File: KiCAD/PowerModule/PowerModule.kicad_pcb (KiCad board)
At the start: 2 copper layers, 90 x 70 mm, 59 parts, among them J2 BATTERY, J3 BUS, J4 MONITOR, Q1 TK8S06K3L, Q2 TK8S06K3L, Q3 AO3401A, Q5 AO3401A, U2 INA219BxDCN, U3 INA219BxDCN, U4 INA219BxDCN, U5 NJM7812SDL1, U6 NJM7812SDL1, U7 NJM7812SDL1, U8 INA219BxDCN

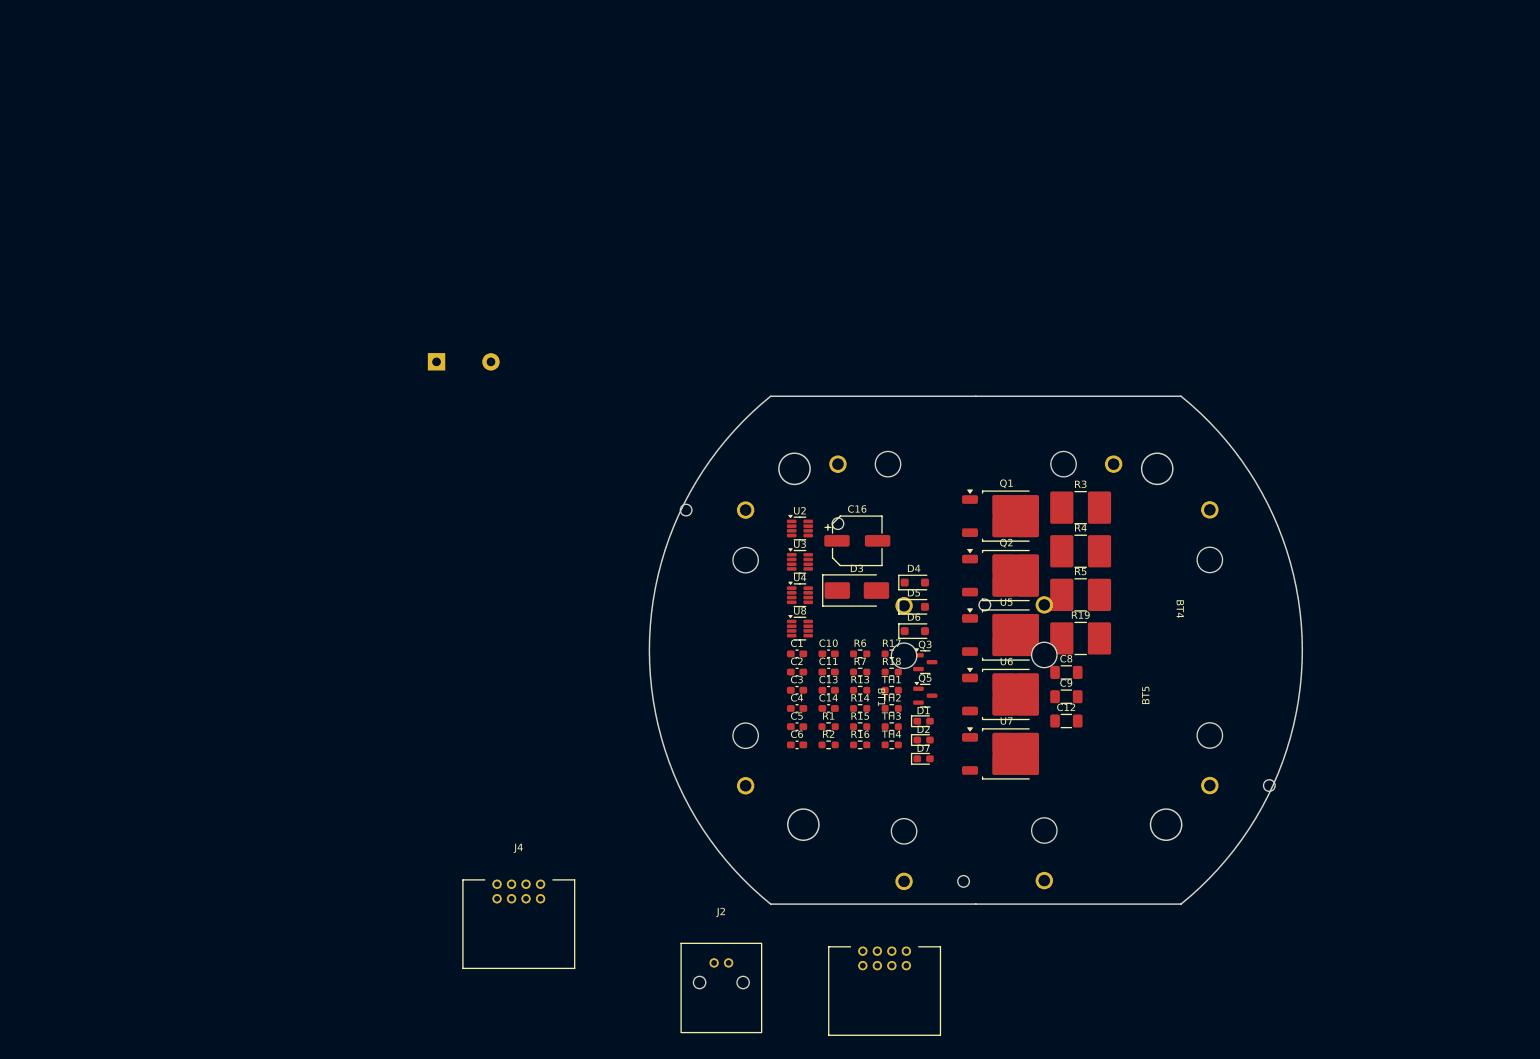
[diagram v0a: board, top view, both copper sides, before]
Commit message: BatteryModule追加＆電池設置
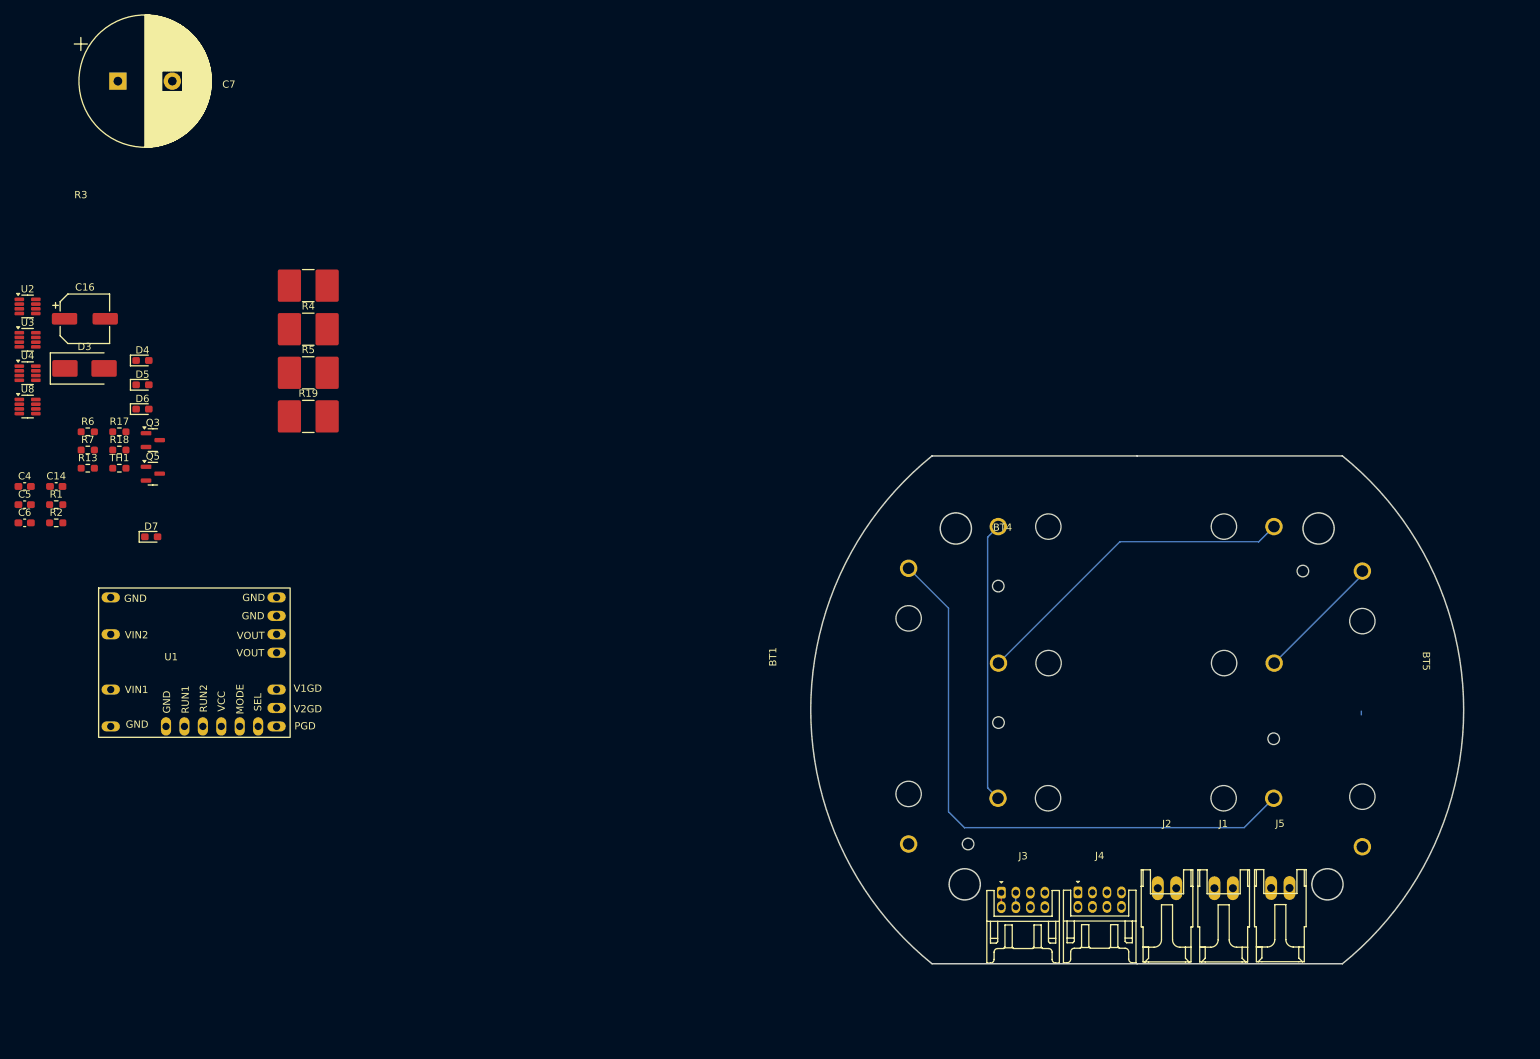
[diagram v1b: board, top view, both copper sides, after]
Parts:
- removed C1, C10, C11, C13: 0.1uF, Capacitor_SMD:C_0603_1608Metric_Pad1.08x0.95mm_HandSolder
- removed C12, C8, C9: 10uF, Capacitor_SMD:C_1206_3216Metric_Pad1.33x1.80mm_HandSolder
- removed C2, C3: 0.056uF, Capacitor_SMD:C_0603_1608Metric_Pad1.08x0.95mm_HandSolder
- removed D1, D2: Orange, LED_SMD:LED_0603_1608Metric_Pad1.05x0.95mm_HandSolder
- removed Q1, Q2: TK8S06K3L, Package_TO_SOT_SMD:TO-252-2
- removed R14, R15, R16, TH2, TH3, TH4: 10kR, Resistor_SMD:R_0603_1608Metric_Pad0.98x0.95mm_HandSolder
- removed U5, U6, U7: NJM7812SDL1, Package_TO_SOT_SMD:TO-252-2
- added J1: GPU, TSRP_Connector_Hirose:DF1B-2S-2.5R, F.Cu at (183.3, 134.4)
- added J5: MASTER, TSRP_Connector_Hirose:DF1B-2S-2.5R, F.Cu at (191.1, 134.4)
- added U1: ~, TSRP_IC:StrawberryLinux_LTC3118, F.Cu at (38.3, 102.3)
- C7: moved to F.Cu
- D4, D5, D6: value GS1010FL -> Orange; footprint Diode_SMD:D_SOD-123F -> LED_SMD:LED_0603_1608Metric_Pad1.05x0.95mm_HandSolder
- J2: footprint TSRP_Connector_Hirose:DF51-2P-2DS -> TSRP_Connector_Hirose:DF1B-2S-2.5R
- J3, J4: footprint TSRP_Connector_Hirose:DF51A-8DP-2DS -> TSRP_Connector_Hirose:DF11-8DP-2DS
- moved C16 110.8 mm to (26.4, 55.2)
- moved C4 110.8 mm to (18.1, 78.3)
- moved C5 110.8 mm to (18.1, 80.8)
- moved C6 110.8 mm to (18.1, 83.3)
- moved D3 110.8 mm to (26.3, 62.0)
- moved D4 110.8 mm to (34.3, 60.9)
- moved D5 110.8 mm to (34.3, 64.3)
- moved D6 110.8 mm to (34.3, 67.6)
- moved D7 110.8 mm to (35.5, 85.2)
- moved R17 110.8 mm to (31.1, 70.8)
- moved R18 110.8 mm to (31.1, 73.3)
- moved R19 110.8 mm to (57.2, 68.6)
- moved R3 110.8 mm to (57.2, 50.6)
- moved R4 110.8 mm to (57.2, 56.6)
- moved R5 110.8 mm to (57.2, 62.6)
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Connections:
- D4 pad 1: +VSW -> Net-(D4-K)
- D5 pad 1: +VSW -> Net-(D5-K)
- D5 pad 2: Net-(D4-A) -> Net-(D5-A)
- D6 pad 1: +VSW -> Net-(D6-K)
- D6 pad 2: Net-(D4-A) -> Net-(D6-A)
- R4 pad 1: Net-(D4-A) -> +VSW
- U8 pad 1: Net-(D4-A) -> +VSW
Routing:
- net Net-(BT1--): track 0.00 -> 83.2 mm
- net Net-(BT3--): track 0.00 -> 45.8 mm
- net Net-(BT2--): track 0.00 -> 38.6 mm
- net Net-(BT4--): track 0.00 -> 18.2 mm
- net GND: track 0.00 -> 2.00 mm
- net +12V: track 0.00 -> 2.00 mm

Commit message: PowerModule基板に収まりました。配線検討中
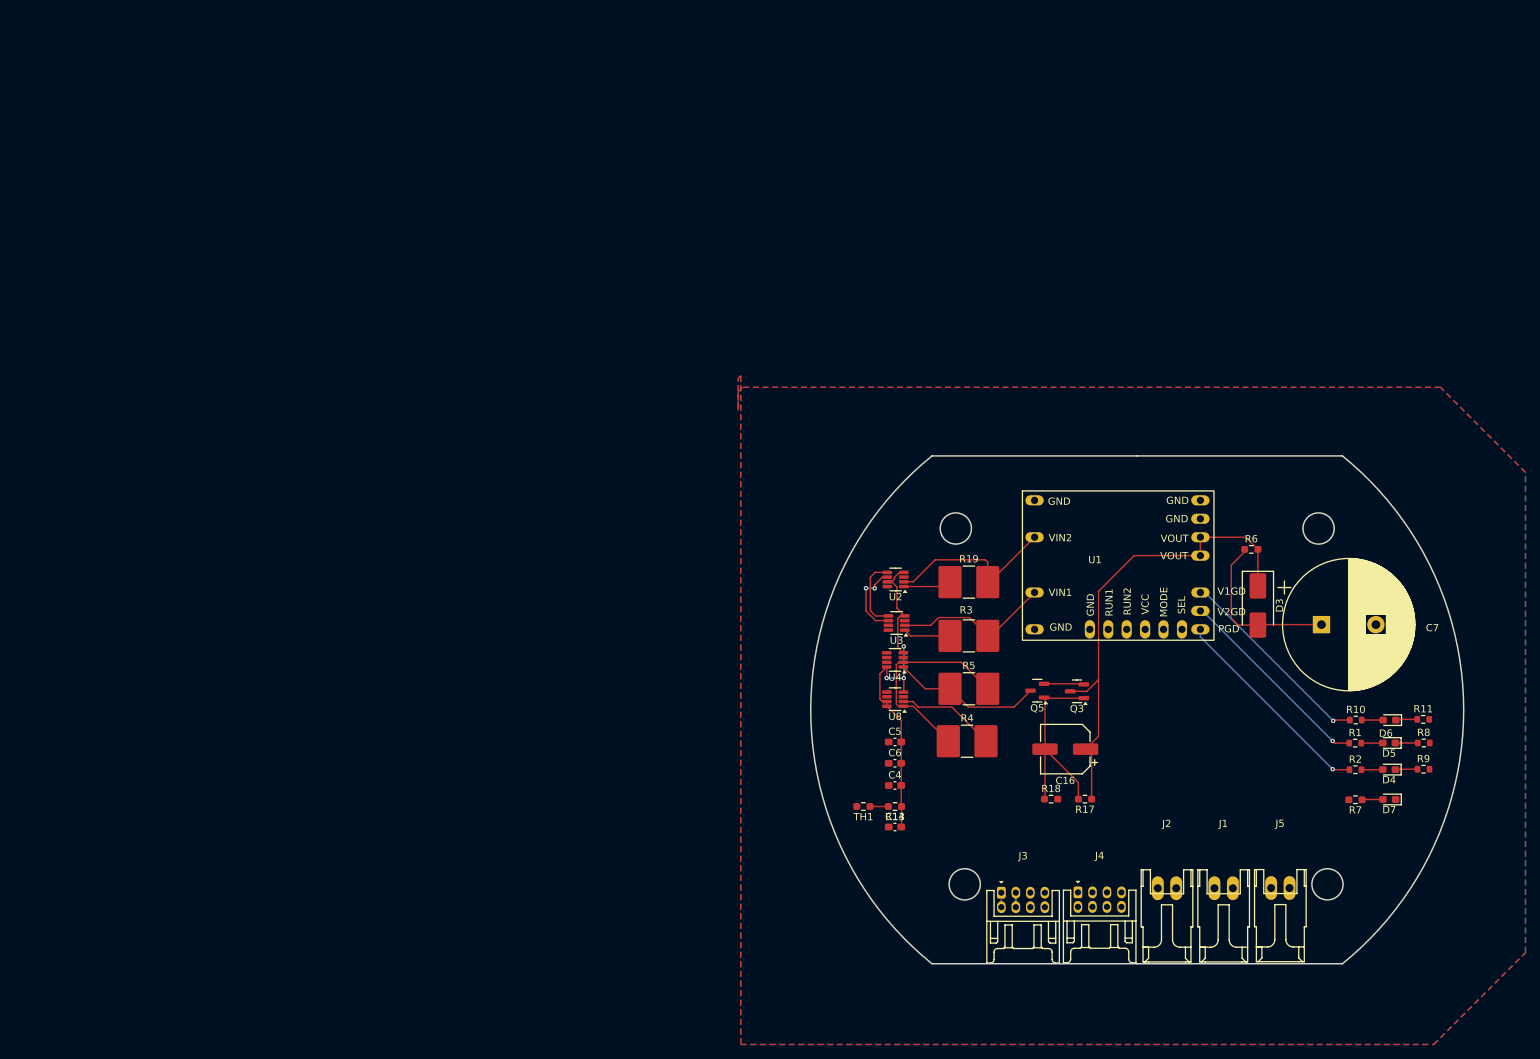
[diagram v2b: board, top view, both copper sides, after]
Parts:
- removed BT1, BT2, BT3, BT4, BT5: CR123A, TSRP_Battery:BHC-CR123A
- added R10: 10k, Resistor_SMD:R_0603_1608Metric, F.Cu at (201.6, 110.5)
- added R11: 1k, Resistor_SMD:R_0603_1608Metric, F.Cu at (210.9, 110.4)
- added R8: 1k, Resistor_SMD:R_0603_1608Metric, F.Cu at (210.9, 113.7)
- added R9: 1k, Resistor_SMD:R_0603_1608Metric, F.Cu at (210.9, 117.3)
- R1, R2: value 2.7kR -> 10k; footprint Resistor_SMD:R_0603_1608Metric_Pad0.98x0.95mm_HandSolder -> Resistor_SMD:R_0603_1608Metric
- moved R2 182.3 mm to (201.5, 117.3)
- moved R1 182.0 mm to (201.5, 113.7)
- moved C7 182.0 mm to (196.9, 97.3)
- moved R7 181.3 mm to (201.5, 121.5), turned to 180 degrees
- moved D4 180.9 mm to (206.2, 117.3), turned to 180 degrees
- moved D5 178.8 mm to (206.2, 113.7), turned to 180 degrees
- moved D6 177.2 mm to (206.2, 110.5), turned to 180 degrees
- moved D7 174.5 mm to (206.2, 121.4), turned to 180 degrees
- moved D3 165.0 mm to (188.1, 94.7), turned to -90 degrees
- moved R6 161.2 mm to (187.2, 87.0)
- moved C16 147.6 mm to (161.5, 114.5), turned to 180 degrees
- moved R17 142.4 mm to (164.2, 121.4), turned to 180 degrees
- moved R18 137.2 mm to (159.6, 121.4)
- moved Q3 132.0 mm to (163.1, 106.5), turned to 180 degrees
- moved U1 128.0 mm to (165.6, 88.9)
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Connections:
- J2 pad 1: Net-(BT1-+) -> +15V
- R1 pad 1: Net-(D1-A) -> Net-(U1-V2GD)
- R1 pad 2: Net-(D3-K) -> Net-(D5-A)
- R2 pad 1: Net-(D2-A) -> Net-(U1-PGD)
- R2 pad 2: Net-(D3-K) -> Net-(D4-A)
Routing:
- net Net-(BT1--): track 83.2 -> 0.00 mm
- net Net-(D3-K): track 0.00 -> 66.8 mm
- net +3.3V: track 0.00 -> 49.8 mm, vias 0 -> 3
- net Net-(BT3--): track 45.8 -> 0.00 mm
- net Net-(BT2--): track 38.6 -> 0.00 mm
- net Net-(U1-PGD): track 0.00 -> 29.2 mm, vias 0 -> 1
- net +VSW: track 0.00 -> 29.0 mm
- net Net-(Q3-G): track 0.00 -> 28.6 mm
- net Net-(U1-V2GD): track 0.00 -> 28.1 mm, vias 0 -> 1
- net Net-(U1-V1GD): track 0.00 -> 28.0 mm, vias 0 -> 1
- net Net-(U1-RUN2): track 0.00 -> 24.7 mm
- net Net-(D3-A): track 0.00 -> 23.1 mm
- net Net-(U1-RUN1): track 0.00 -> 21.9 mm
- net Net-(Q5-S): track 0.00 -> 20.8 mm
- net Net-(BT4--): track 18.2 -> 0.00 mm
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- added copper zone on B.Cu, net GND
- added copper zone on F.Cu, net GND

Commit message: 配線の確認お願いします
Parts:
- removed C14: 0.1uF, Capacitor_SMD:C_0603_1608Metric_Pad1.08x0.95mm_HandSolder
- removed R4: 0.1R, Resistor_SMD:R_2816_7142Metric_Pad3.20x4.45mm_HandSolder
- removed U8: INA219BxDCN, Package_TO_SOT_SMD:SOT-23-8
- added J6: Conn_01x02, TSRP_Connector_Hirose:DF1B-2S-2.5R, F.Cu at (133.0, 125.0)
- added REF**: MountingHole_3.2mm_M3_DIN965_Pad_TopBottom, MountingHole:MountingHole_3.2mm_M3_DIN965_Pad_TopBottom, F.Cu at (125.0, 125.0)
- added REF**: MountingHole_3.2mm_M3_DIN965_Pad_TopBottom, MountingHole:MountingHole_3.2mm_M3_DIN965_Pad_TopBottom, F.Cu at (125.0, 75.0)
- added REF**: MountingHole_3.2mm_M3_DIN965_Pad_TopBottom, MountingHole:MountingHole_3.2mm_M3_DIN965_Pad_TopBottom, F.Cu at (175.0, 125.0)
- added REF**: MountingHole_3.2mm_M3_DIN965_Pad_TopBottom, MountingHole:MountingHole_3.2mm_M3_DIN965_Pad_TopBottom, F.Cu at (175.0, 75.0)
- R7: moved to B.Cu
- moved J5 82.8 mm to (133.6, 74.8), turned to 180 degrees
- moved J1 72.7 mm to (141.7, 74.8), turned to 180 degrees
- moved R17 51.8 mm to (164.7, 69.6)
- moved R18 51.8 mm to (160.0, 69.6), turned to 180 degrees
- moved R7 45.1 mm to (156.6, 125.5), turned to 90 degrees
- moved C16 38.8 mm to (163.7, 75.8)
- moved D7 37.8 mm to (170.0, 132.2), turned to 90 degrees
- moved J2 35.8 mm to (141.0, 125.0)
- moved R9 31.3 mm to (179.7, 119.6), turned to -90 degrees
- moved R8 28.1 mm to (183.7, 120.6), turned to -90 degrees
- moved D4 27.4 mm to (178.8, 116.7)
- moved R1 27.1 mm to (174.5, 112.9)
- moved R2 27.1 mm to (174.5, 116.6)
- moved R10 27.1 mm to (174.5, 109.7)
- moved R11 25.4 mm to (187.6, 120.6), turned to -90 degrees
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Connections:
- J2 pad 1: +15V -> Net-(J2-Pin_1)
- R5 pad 2: +VSW -> +12V
- U4 pad 2: +VSW -> +12V
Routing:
- net I2C_SCL: track 10.0 -> 83.3 mm
- net Net-(Q5-S): track 20.8 -> 65.0 mm, vias 0 -> 4
- net I2C_SDA: track 10.6 -> 49.6 mm, vias 2 -> 4
- net Net-(J1-Pin_2): track 6.56 -> 39.6 mm, vias 0 -> 2
- net Net-(J5-Pin_2): track 0.00 -> 31.3 mm
- net Net-(U1-RUN1): track 21.9 -> 52.1 mm, vias 0 -> 1
- net +VSW: track 29.0 -> 0.00 mm
- net Net-(U1-PGD): track 29.2 -> 4.07 mm, vias 1 -> 0
- net Net-(U1-V1GD): track 28.0 -> 3.39 mm, vias 1 -> 0
- net Net-(U1-V2GD): track 28.1 -> 3.58 mm, vias 1 -> 0
- net Net-(D3-K): track 66.8 -> 44.2 mm
- net Net-(U1-RUN2): track 24.7 -> 46.3 mm
- net Net-(D7-A): track 2.90 -> 16.8 mm, vias 0 -> 1
- net +3.3V: track 49.8 -> 63.1 mm, vias 3 -> 2
- net Net-(J2-Pin_2): track 6.62 -> 19.8 mm
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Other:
- board text added: "10k"
- board text added: "1k"
- board text added: "AVAILABLE"
- board text added: "BAT SW"
- board text added: "BATTERY"
- board text added: "BUS"
- board text added: "EXT"
- board text added: "Greeeeeen"
- board text added: "LTC3118"
- board text added: "MONITOR"
- board text added: "P2GD"
- board text added: "PGD"
- board text added: "SW"
- board text added: "V1GD"
- board text added: "orange"

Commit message: 配線完了
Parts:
- removed C7: 2200uF, Capacitor_THT:CP_Radial_D18.0mm_P7.50mm
- removed REF** (x4): MountingHole_3.2mm_M3_DIN965_Pad_TopBottom, MountingHole:MountingHole_3.2mm_M3_DIN965_Pad_TopBottom
- added H1: MountingHole, MountingHole:MountingHole_3.2mm_M3_DIN965_Pad_TopBottom, F.Cu at (125.0, 125.0)
- added H2: MountingHole, MountingHole:MountingHole_3.2mm_M3_DIN965_Pad_TopBottom, F.Cu at (125.0, 75.0)
- added H3: MountingHole, MountingHole:MountingHole_3.2mm_M3_DIN965_Pad_TopBottom, F.Cu at (175.0, 125.0)
- added H4: MountingHole, MountingHole:MountingHole_3.2mm_M3_DIN965_Pad_TopBottom, F.Cu at (175.0, 75.0)
- added J7: Conn_01x02, TSRP_Connector_Hirose:DF1B-2S-2.5R, F.Cu at (143.0, 75.0)
- TH1: footprint Resistor_SMD:R_0603_1608Metric_Pad0.98x0.95mm_HandSolder -> Connector_PinHeader_1.00mm:PinHeader_1x02_P1.00mm_Vertical
- moved J6 53.5 mm to (152.0, 75.0), turned to 180 degrees
- moved J2 50.5 mm to (134.0, 75.0), turned to 180 degrees
- moved J1 50.4 mm to (137.0, 125.0), turned to 0 degrees
- moved U4 40.5 mm to (123.5, 95.1)
- moved R3 29.9 mm to (140.9, 119.1)
- moved R19 29.8 mm to (135.3, 85.7), turned to 0 degrees
- moved J5 26.5 mm to (160.0, 75.0)
- moved Q5 26.2 mm to (175.0, 102.9), turned to 90 degrees
- moved Q3 19.0 mm to (175.0, 96.9), turned to 90 degrees
- moved C5 17.9 mm to (131.7, 94.1), turned to 180 degrees
- moved U2 14.5 mm to (123.6, 100.5)
- moved TH1 13.9 mm to (143.5, 132.0), turned to -90 degrees
- moved R17 13.4 mm to (164.0, 83.0), turned to 0 degrees
- moved C16 13.3 mm to (162.0, 89.0), turned to 0 degrees
- moved R18 12.1 mm to (164.0, 81.0)
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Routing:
- net +12V: track 10.9 -> 64.9 mm, vias 0 -> 2
- net Net-(J5-Pin_2): track 31.3 -> 7.73 mm
- net Net-(Q5-S): track 65.0 -> 86.0 mm, vias 4 -> 3
- net VREF_T1: track 6.92 -> 26.9 mm
- net Net-(U1-RUN2): track 46.3 -> 65.6 mm, vias 0 -> 1
- net Net-(J2-Pin_1): track 5.46 -> 18.7 mm
- net I2C_SCL: track 83.3 -> 70.2 mm, vias 0 -> 3
- net Net-(J2-Pin_2): track 19.8 -> 32.0 mm, vias 0 -> 2
- net I2C_SDA: track 49.6 -> 60.9 mm
- net Net-(J1-Pin_2): track 39.6 -> 29.3 mm, vias 2 -> 1
- net Net-(Q3-G): track 18.3 -> 28.0 mm
- net +5V: track 0.00 -> 8.00 mm
- net Net-(D3-K): track 44.2 -> 48.6 mm, vias 0 -> 1
- net +3.3V: track 63.1 -> 67.1 mm, vias 2 -> 1
- net Net-(D3-A): track 16.1 -> 19.5 mm
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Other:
- outline, holes or cut-outs redrawn
- board text added: "capacitor"
- board text removed: "Greeeeeen"
- board text removed: "orange"
